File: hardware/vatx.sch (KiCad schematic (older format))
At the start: 27 parts, among them J1 USB, P1 CONN_10X2, P10 CONN_1, P11 CONN_1, P2 CONN_1, P3 CONN_1, P4 CONN_1, P5 CONN_1, P6 CONN_1, P7 CONN_1, P8 CONN_1, P9 CONN_1, SW1 SWITCH_INV, U1 LM317T

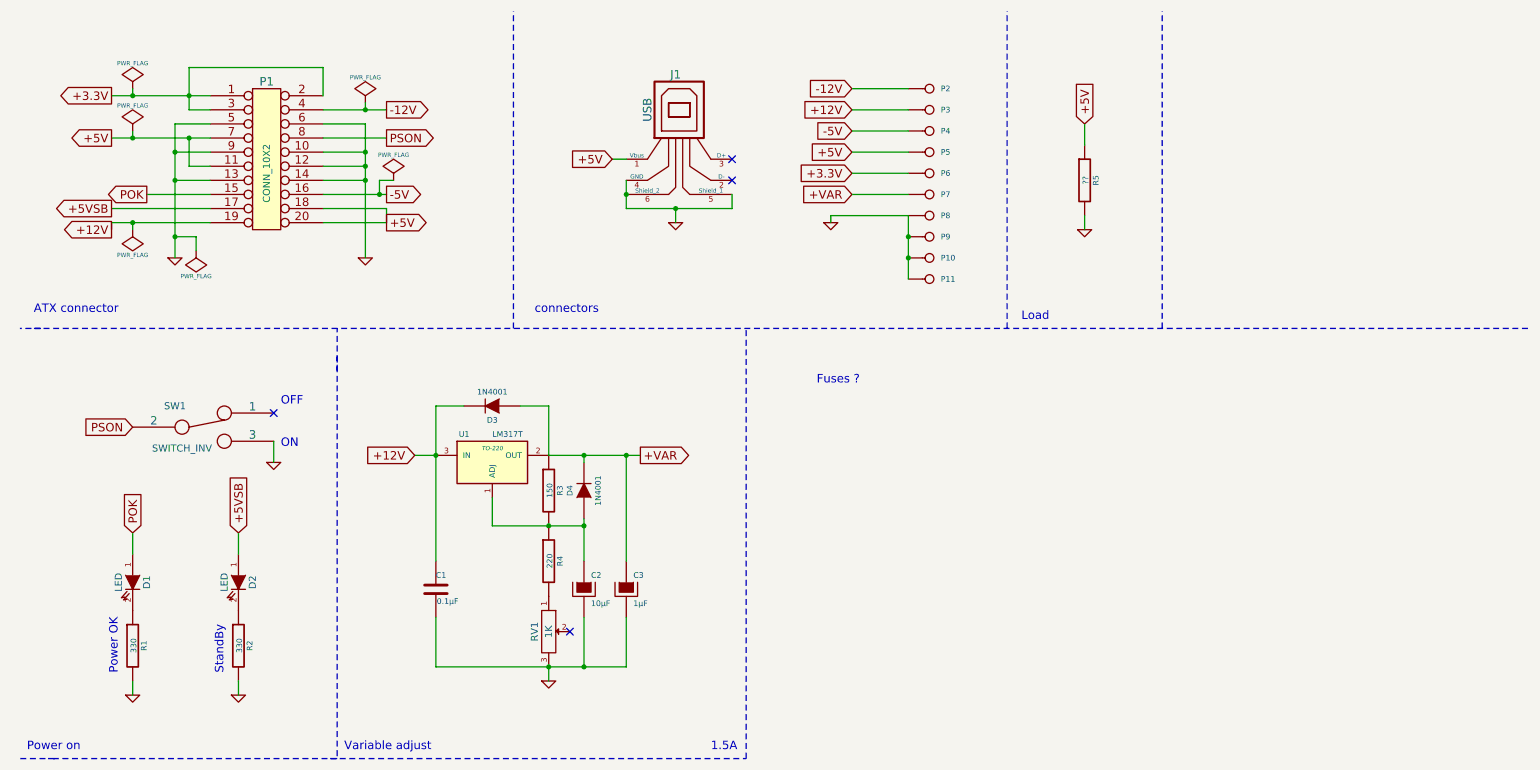
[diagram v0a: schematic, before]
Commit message: Move to a smaller board * remove load resistor * remove -5 / -12 * 50x50mm pcb * SMD components for seeedstudio OPL
TODO:
* switch footprint
* check diodes footprint
* silkscreen
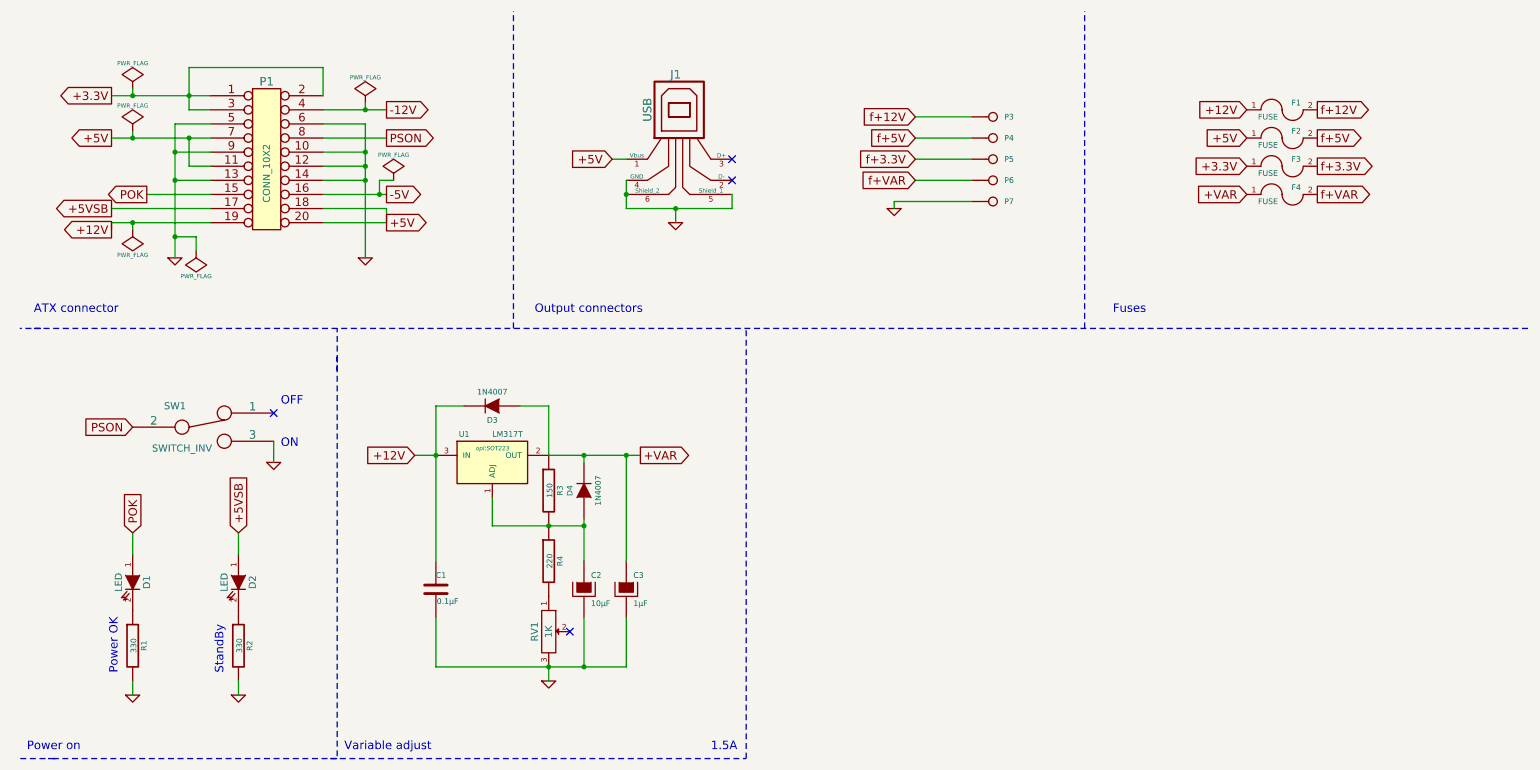
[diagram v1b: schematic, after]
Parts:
- removed P10, P11, P2, P4, P9: CONN_1, symbol CONN_1
- removed R5: ??, symbol R
- added F1, F2, F3, F4: FUSE, SMD_Packages:SMD-1206, symbol FUSE
- C1: footprint (none) -> SMD_Packages:SMD-0603_c
- C2, C3: footprint (none) -> SMD_Packages:SMD-0805
- D1, D2: footprint (none) -> LEDs:LED-0603
- D3, D4: value 1N4001 -> 1N4007; footprint (none) -> Diodes_SMD:Diode-MELF_Standard
- J1: footprint (none) -> atx:USB_A_DOUBLE
- P1: footprint (none) -> atx:ATX_NON_90DEG
- P3: footprint (none) -> atx:Banana_single_6mmDrill
- P4: renamed from P5; footprint (none) -> atx:Banana_single_6mmDrill
- P5: renamed from P6; footprint (none) -> atx:Banana_single_6mmDrill
- P6: renamed from P7; footprint (none) -> atx:Banana_single_6mmDrill
- P7: renamed from P8; footprint (none) -> atx:Banana_single_6mmDrill
- R1, R2, R3, R4: footprint (none) -> Resistors_SMD:R_0603
- RV1: footprint (none) -> Potentiometers:Potentiometer_Alps-RK16-single_largePads
- SW1: footprint (none) -> Discret:MICROSWITCH_SPST
- U1: footprint TO-220 -> opl:SOT223
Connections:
- net +12V: now also F1.1; no longer P3.1
- net +3.3V: now also F3.1; no longer P5.1
- net +5V: now also F2.1; no longer P4.1
- net +VAR: now also F4.1; no longer P6.1
- new net f+12V: F1.2, P3.1
- new net f+3.3V: F3.2, P5.1
- new net f+5V: F2.2, P4.1
- new net f+VAR: F4.2, P6.1
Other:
- note added: "Fuses"
- note added: "Output connectors"
- note removed: "Fuses ?"
- note removed: "Load"
- note removed: "connectors"
- moved on the sheet: P3, P4, P5, P6, P7

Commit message: Short between D+/D- to be an USB DCP http://www.maximintegrated.com/en/app-notes/index.mvp/id/4803
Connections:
- net at J1.2 (D-): now also J1.3 (D+)
- no-connect marks 4 -> 2
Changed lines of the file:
@@
 	5550 1900 5550 1800
 Connection ~ 5150 1900
-NoConn ~ 5550 1700
-NoConn ~ 5550 1550
 $Comp
 L FUSE F1
@@
 Wire Notes Line
 	8050 2750 8050 500
+Wire Wire Line
+	5550 1550 5550 1700
 $EndSCHEMATC

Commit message: room for 24pins ATX connector seeed opl switch footprint seeed opl usb A footprint fused +5V for usb leds on/power labels paste for heatsink
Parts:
- J1: footprint atx:USB_A_DOUBLE -> opl:4P-2.0-90D
- SW1: footprint Discret:MICROSWITCH_SPST -> opl:TS-1101F
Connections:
- net +5V: no longer J1.1 (Vbus)
- net f+5V: now also J1.1 (Vbus)
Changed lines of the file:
@@
 F 0 "SW1" H 1600 3600 50  0000 C CNN
 F 1 "SWITCH_INV" H 1650 3300 50  0000 C CNN
-F 2 "Discret:MICROSWITCH_SPST" H 1800 3450 60  0001 C CNN
+F 2 "opl:TS-1101F" H 1800 3450 60  0001 C CNN
 F 3 "" H 1800 3450 60  0000 C CNN
 	1    1800 3450
@@
 	6700 1850 6700 1900
 Text GLabel 4700 1550 0    60   Input ~ 0
-+5V
+f+5V
 $Comp
 L GND #PWR08
@@
 F 0 "J1" H 5150 1750 60  0000 C CNN
 F 1 "USB" V 4950 1500 60  0000 C CNN
-F 2 "atx:USB_A_DOUBLE" H 5200 1350 60  0001 C CNN
+F 2 "opl:4P-2.0-90D" H 5200 1350 60  0001 C CNN
 F 3 "" H 5200 1350 60  0000 C CNN
 	1    5200 1350

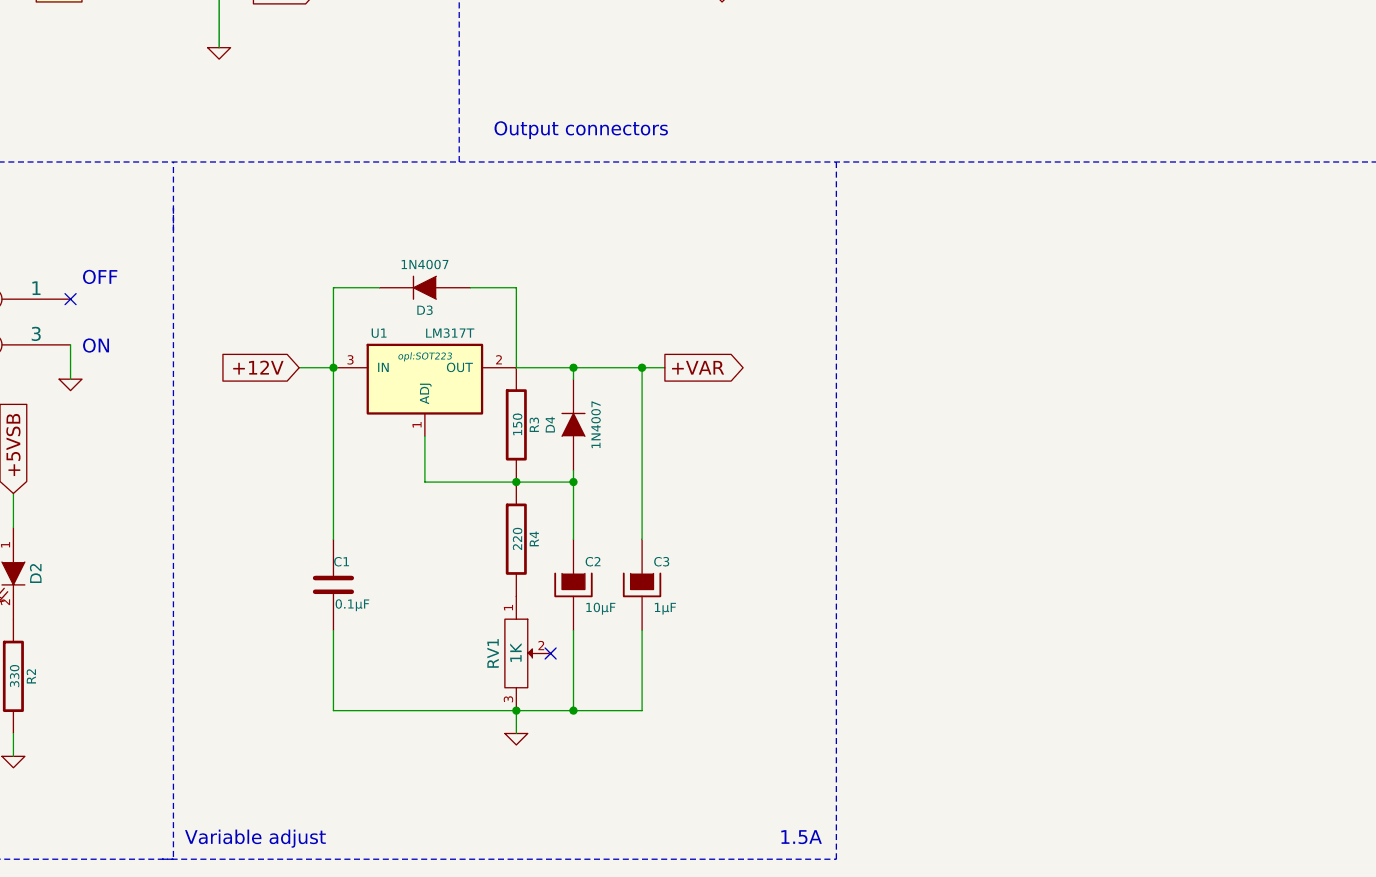
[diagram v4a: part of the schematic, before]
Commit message: Add power resistor some PSU need that to deliver current
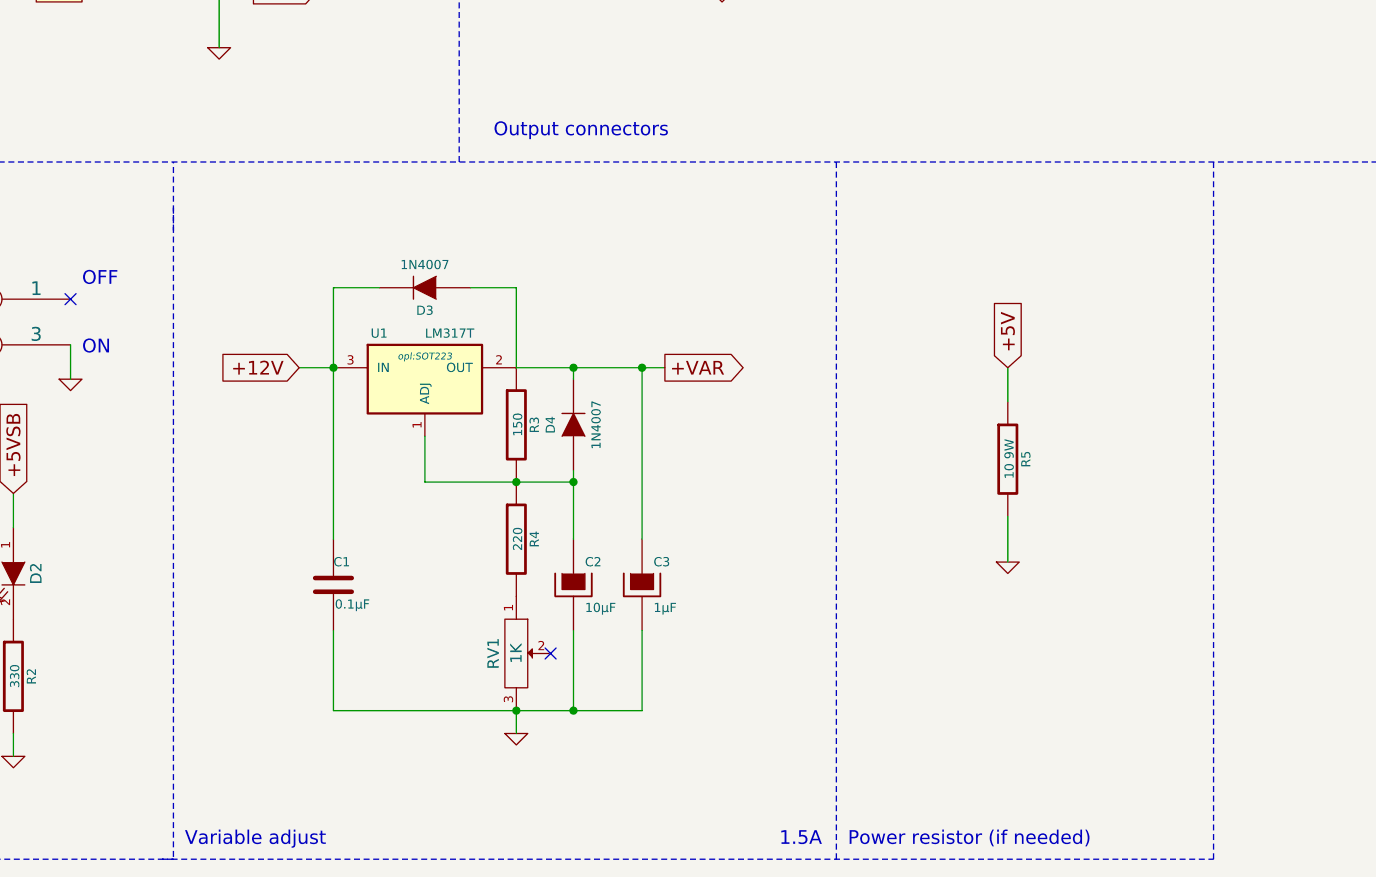
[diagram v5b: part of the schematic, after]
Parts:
- added R5: 10 9W, Resistors_ThroughHole:Resistor_Horizontal_RM25mm, symbol R
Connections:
- net +5V: now also R5.1
- net GND: now also R5.2
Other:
- note added: "Power resistor (if needed)"
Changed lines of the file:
@@
 Power on
 Wire Notes Line
-	2700 5800 5650 5800
+	2700 5800 7300 5800
 Wire Notes Line
 	5650 5800 5650 2750
@@
 Wire Wire Line
 	5550 1550 5550 1700
+Text GLabel 6400 3650 1    60   Input ~ 0
++5V
+$Comp
+L R R5
+U 1 1 54FF3F0D
+P 6400 4050
+F 0 "R5" V 6480 4050 40  0000 C CNN
+F 1 "10 9W" V 6407 4051 40  0000 C CNN
+F 2 "Resistors_ThroughHole:Resistor_Horizontal_RM25mm" V 6330 4050 30  0001 C CNN
+F 3 "" H 6400 4050 30  0000 C CNN
+	1    6400 4050
+	1    0    0    -1
+$EndComp
+$Comp
+L GND #PWR015
+U 1 1 54FF3F8D
+P 6400 4500
+F 0 "#PWR015" H 6400 4500 30  0001 C CNN
+F 1 "GND" H 6400 4430 30  0001 C CNN
+F 2 "" H 6400 4500 60  0000 C CNN
+F 3 "" H 6400 4500 60  0000 C CNN
+	1    6400 4500
+	1    0    0    -1
+$EndComp
+Wire Wire Line
+	6400 3650 6400 3800
+Wire Wire Line
+	6400 4300 6400 4500
+Wire Notes Line
+	7300 5800 7300 2750
+Text Notes 5700 5750 0    60   ~ 0
+Power resistor (if needed)
 $EndSCHEMATC

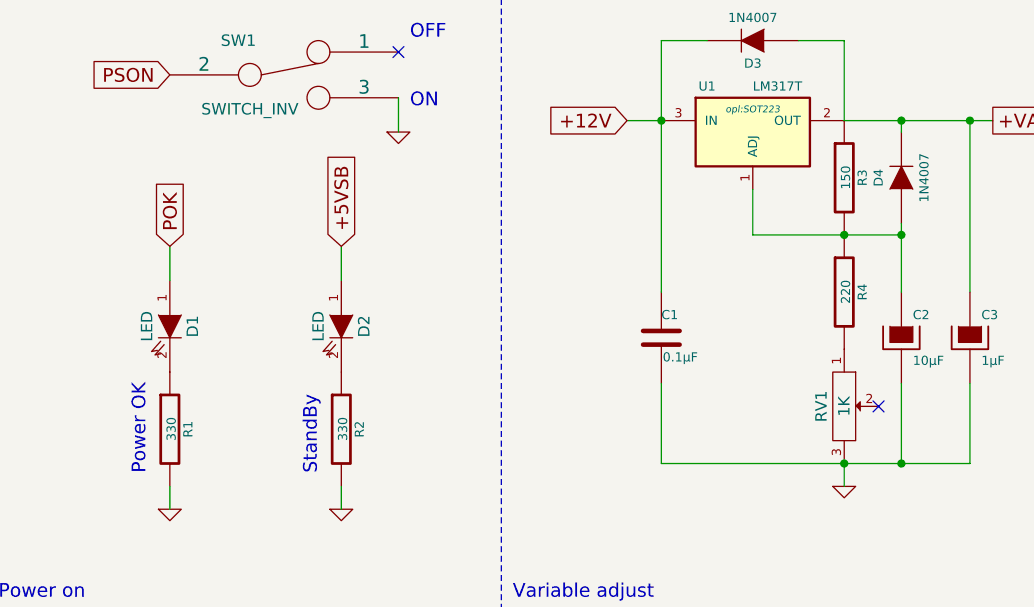
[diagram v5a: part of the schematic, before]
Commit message: Update +VAR : remove R4 R1/R2 values updated for choosen leds Seeed BOM
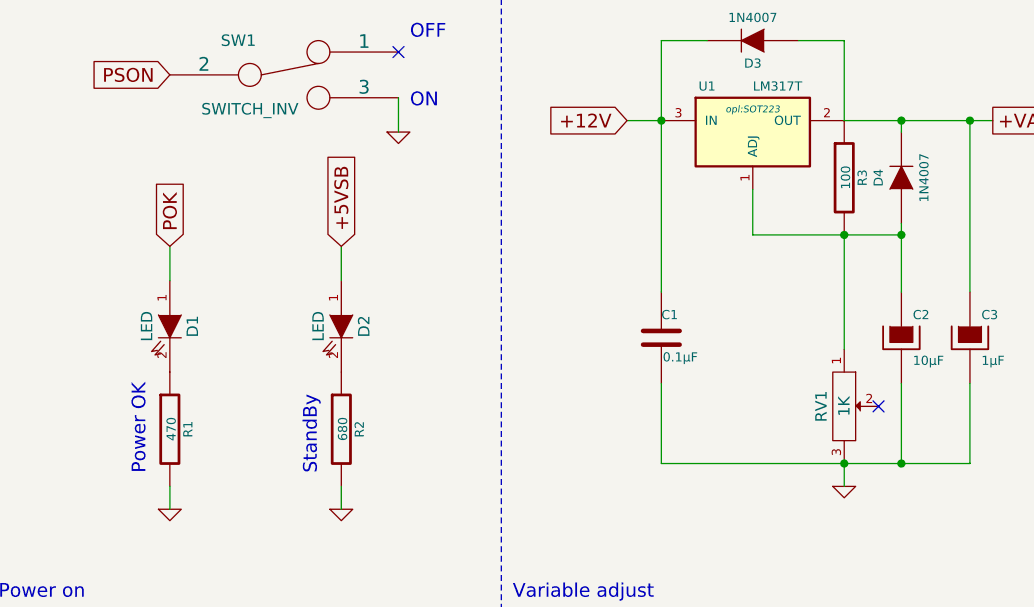
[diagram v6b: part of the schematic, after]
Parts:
- removed R4: 220, Resistors_SMD:R_0603, symbol R
- R1: value 330 -> 470
- R2: value 330 -> 680
- R3: value 150 -> 100
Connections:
- net at C2.1, D4.1 (A), R3.2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: now also RV1.1
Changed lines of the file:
@@
 P 1300 5000
 F 0 "R1" V 1380 5000 40  0000 C CNN
-F 1 "330" V 1307 5001 40  0000 C CNN
+F 1 "470" V 1307 5001 40  0000 C CNN
 F 2 "Resistors_SMD:R_0603" V 1230 5000 30  0001 C CNN
 F 3 "" H 1300 5000 30  0000 C CNN
@@
 P 2050 5000
 F 0 "R2" V 2130 5000 40  0000 C CNN
-F 1 "330" V 2057 5001 40  0000 C CNN
+F 1 "680" V 2057 5001 40  0000 C CNN
 F 2 "Resistors_SMD:R_0603" V 1980 5000 30  0001 C CNN
 F 3 "" H 2050 5000 30  0000 C CNN
@@
 P 4250 3900
 F 0 "R3" V 4330 3900 40  0000 C CNN
-F 1 "150" V 4257 3901 40  0000 C CNN
+F 1 "100" V 4257 3901 40  0000 C CNN
 F 2 "Resistors_SMD:R_0603" V 4180 3900 30  0001 C CNN
 F 3 "" H 4250 3900 30  0000 C CNN
 	1    4250 3900
-	1    0    0    -1
-$EndComp
-$Comp
-L R R4
-U 1 1 5345CF33
-P 4250 4400
-F 0 "R4" V 4330 4400 40  0000 C CNN
-F 1 "220" V 4257 4401 40  0000 C CNN
-F 2 "Resistors_SMD:R_0603" V 4180 4400 30  0001 C CNN
-F 3 "" H 4250 4400 30  0000 C CNN
-	1    4250 4400
 	1    0    0    -1
 $EndComp
@@
 Text Notes 5700 5750 0    60   ~ 0
 Power resistor (if needed)
+Wire Wire Line
+	4250 4150 4250 4650
 $EndSCHEMATC

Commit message: documentation
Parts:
- D1: value LED -> blue
- D2: value LED -> yellow
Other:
- note added: "1.25V .. 10V\n1.0A"
- note removed: "1.5A"
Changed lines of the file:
@@
 P 1300 4550
 F 0 "D1" H 1300 4650 50  0000 C CNN
-F 1 "LED" H 1300 4450 50  0000 C CNN
+F 1 "blue" H 1300 4450 50  0000 C CNN
 F 2 "LEDs:LED-0603" H 1300 4550 60  0001 C CNN
 F 3 "" H 1300 4550 60  0000 C CNN
@@
 P 2050 4550
 F 0 "D2" H 2050 4650 50  0000 C CNN
-F 1 "LED" H 2050 4450 50  0000 C CNN
+F 1 "yellow" H 2050 4400 50  0000 C CNN
 F 2 "LEDs:LED-0603" H 2050 4550 60  0001 C CNN
 F 3 "" H 2050 4550 60  0000 C CNN
@@
 	3050 1700 3050 1800
 Connection ~ 3050 1800
-Text Notes 5400 5750 0    60   ~ 0
-1.5A
+Text Notes 5600 5750 2    60   ~ 0
+1.25V ..  10V\n1.0A
 Text Notes 8250 2650 0    60   ~ 0
 Fuses
